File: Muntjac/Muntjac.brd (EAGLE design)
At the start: 56.8 x 34.5 mm, 106 parts, among them U1 CC2538, U10 DMG6602SVT, U11 SN74AVC4T774PW, U12 TMP102AIDRLT, U2 CC1120_RHM_32, U3 TPD2E001IDRLRQ1, U4 CP2103, U5 BSS138PS, U6 BSS138PS, U7 BSS138PS, U8 M25P16VMN6P, U9 DMG6602SVT, X1 FA-128, X2 32MHz, X3 32.768K

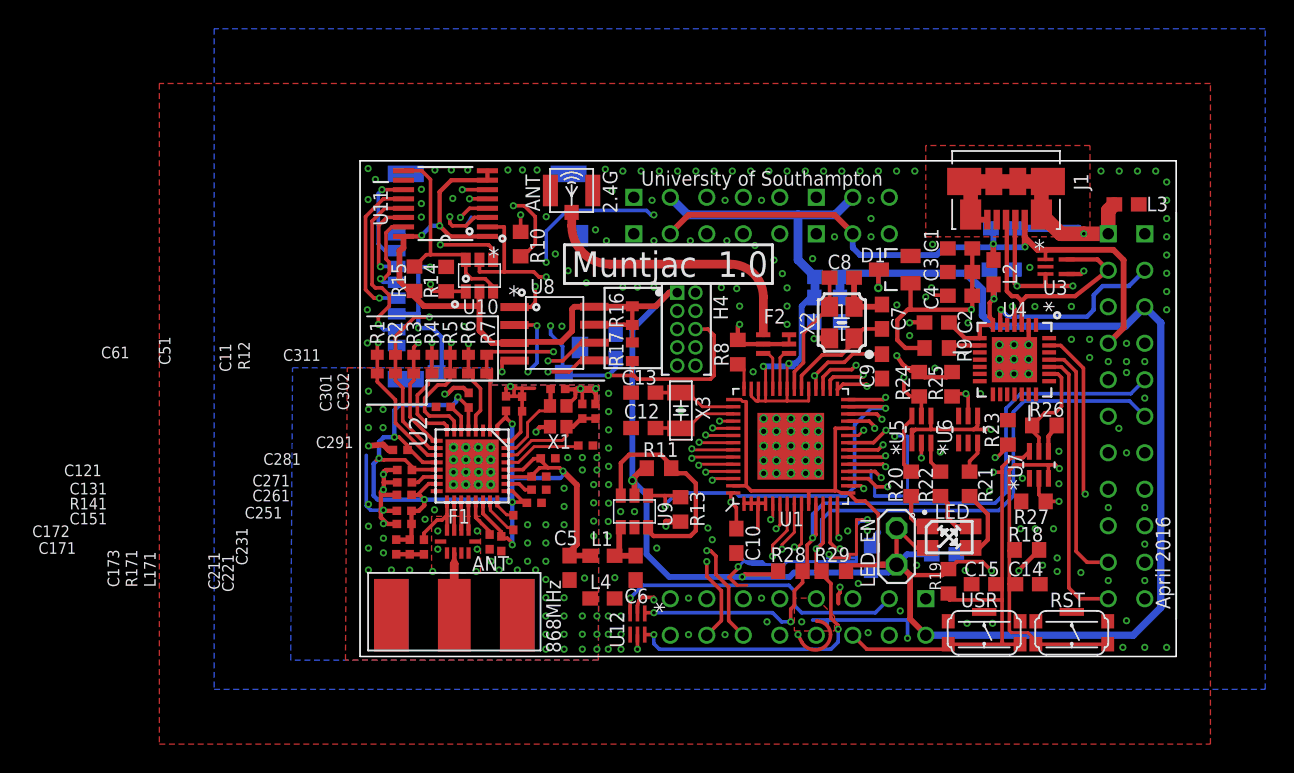
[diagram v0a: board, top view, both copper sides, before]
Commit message: Added LEDs for Serial TX/RX.
brd as submitted for manufacture.
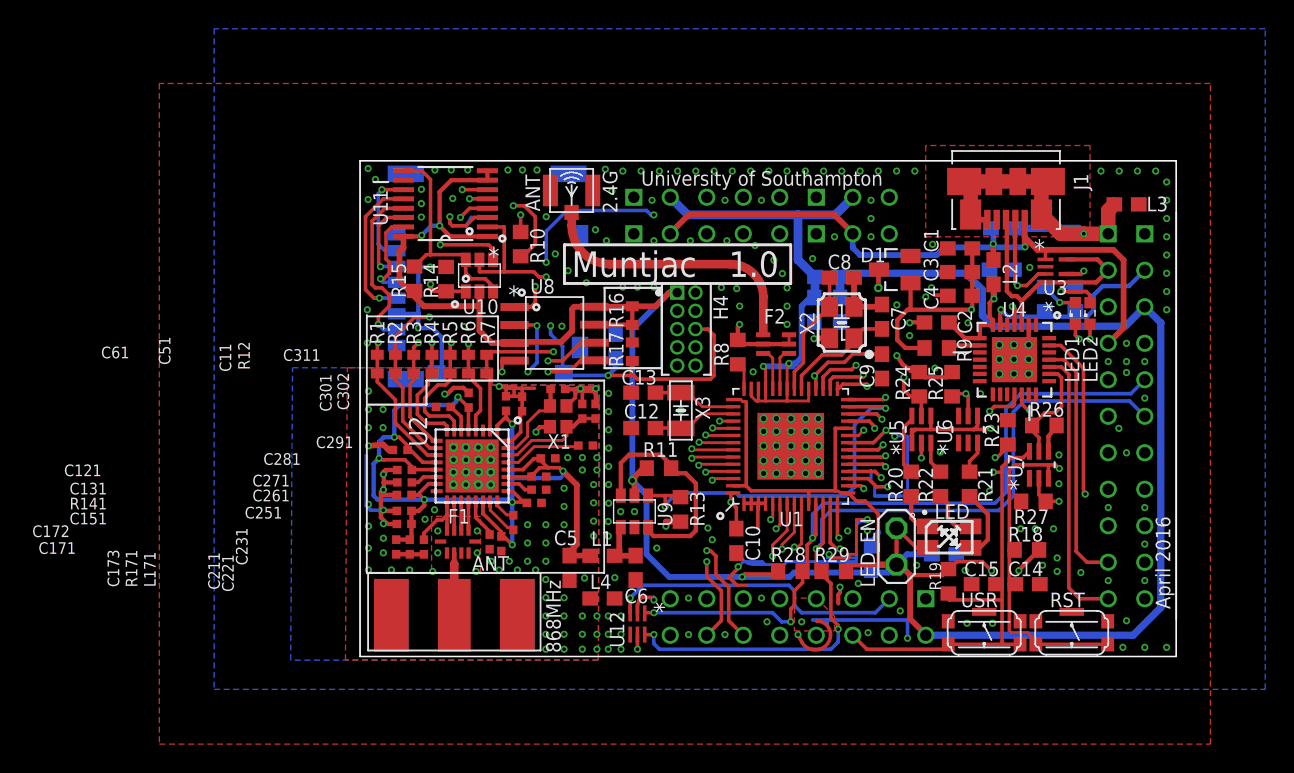
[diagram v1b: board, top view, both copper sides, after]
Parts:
- added LED1, LED2: (no value), led:SML0603
- added R30, R31: 1K5, rcl:R0603
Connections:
- new net N$20: LED1.A, R30.1
- new net N$40: LED2.A, R31.1
- net +3V3_SERIAL: now also R30.2, R31.2
- net N$15: now also LED1.C
- net N$17: now also LED2.C
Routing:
- net N$17: track 0.00 -> 15.8 mm, vias 0 -> 2
- net N$15: track 0.00 -> 10.5 mm, vias 0 -> 2
- net N$40: track 0.00 -> 4.00 mm, vias 0 -> 1
- net N$20: track 0.00 -> 2.70 mm, vias 0 -> 1
- net USB_D_N: track 15.9 -> 17.6 mm, vias 3 -> 2
- net RGND: track 34.5 -> 36.0 mm
- net +3V3_SERIAL: track 31.0 -> 31.8 mm
- net PWR_SENSE_EN: track 81.4 -> 80.8 mm
- net GND: vias 194 -> 188
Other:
- board text added: "Southampton"
- board text added: "University of"

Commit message: Final Muntjac 1.0 commit for manufacture
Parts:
- added C21: 22uF, CC11x:C0603
- moved ANT 0.51 mm to (15.2, 32.4)
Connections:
- net GND: now also C21.2
- net MEM_VCC: now also C21.1
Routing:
- net MEM_VCC: track 24.7 -> 27.9 mm
- net 2.4G: track 19.0 -> 18.4 mm
- net GND: track 168.5 -> 168.4 mm, vias 188 -> 191

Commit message: Added values to schematic for CC1120 layout.
Updated parts list.
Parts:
- C11, C121, C131, C151, C221, C251, C261, C271, C281, C291, C51: value (none) -> 47nF
- C171, C211: value (none) -> 10nF
- C172: value (none) -> 100pF
- C173: value (none) -> 33pF
- C231: value (none) -> 1.8nF
- C301, C311: value (none) -> 15pF
- C302, R12: value (none) -> DNP
- C61: value (none) -> 220nF
- L171: value (none) -> 10n
- R141: value (none) -> 56K
- R171: value (none) -> 10
